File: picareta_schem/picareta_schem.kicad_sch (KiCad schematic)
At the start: 0 parts

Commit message: powertrain
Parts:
- added M1, M2, M3: Motor_DC, symbol Motor:Motor_DC
- added U1, U2, U3: ~, symbol ACC26:ESC
- added U4: ~, symbol library_pic_powertrain:PDB

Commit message: Updat Component's Format
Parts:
- added ADS1220: (no value), symbol Library_Laura_PIC:ADS1220
- added FLC3-1: (no value), symbol Library_Laura_PIC:FLC3-70
- added FLIR_LEPTON_CAMERA1, FLIR_LEPTON_CAMERA2: (no value), symbol Library_Laura_PIC:FLIR_Lepton_250-0577-00_DS_1-2021
- added JetsonOrinNX8GB1: (no value), symbol Library_Laura_PIC:Jetson_Orin_NX_8GB
- U1, U2, U3, U4: value ~ -> (none)

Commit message: Place Components On Schematic
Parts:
- added JetsonOrinNX8GB2: (no value), symbol Library_Laura_PIC:Jetson_Orin_NX_8GB
- added M10Q1: (no value), symbol Library_Laura_PIC:M10Q5883
- added MatekH743-WLITE1: (no value), symbol Library_Laura_PIC:Matek_H743-WLITE
- added RM-2450-12M1: (no value), symbol Library_Laura_PIC:RM-2450-12M3
- added SENTERA_6X_CAMERA1: (no value), symbol Library_Laura_PIC:SENTERA_6X_CAMERA

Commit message: Schematics progress with adjustments on component's pin placement
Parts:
- removed FLIR_LEPTON_CAMERA2: (no value), symbol Library_Laura_PIC:FLIR_Lepton_250-0577-00_DS_1-2021
- removed JetsonOrinNX8GB2: (no value), symbol Library_Laura_PIC:Jetson_Orin_NX_8GB
- added JetsonOrinNX8GB2: (no value), symbol Library_Laura_PIC:Jetson_Orin_NX_8GB_1
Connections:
- net 5V: now reaches U4. (BAT-)
- net 5V: now also ADS1220. (AIN3), FLIR_LEPTON_CAMERA1.2 (PWR_IN), M10Q1. (5V), MatekH743-WLITE1. (GND), RM-2450-12M1. (VDD)
- net SPI_CLK: now reaches ADS1220. (AIN3)
- net SPI_CLK: now also FLIR_LEPTON_CAMERA1.7 (SPI_CLK), MatekH743-WLITE1. (GND), JetsonOrinNX8GB2.91 (SPI0_SCK_)
- net SPI_MOSI: now reaches MatekH743-WLITE1. (GND)
- net SPI_MOSI: now also JetsonOrinNX8GB2.89 (SPI0_MOSI_)
- net GND: now reaches FLIR_LEPTON_CAMERA1.1 (GND)
- net GND: now also ADS1220. (AIN3), FLC3-1. (Z_A3), FLIR_LEPTON_CAMERA1.19 (GND), M10Q1. (5V), MatekH743-WLITE1. (GND), RM-2450-12M1. (VDD), SENTERA_6X_CAMERA1. (VDD-), JetsonOrinNX8GB2.247 (GND), JetsonOrinNX8GB2.249 (GND), JetsonOrinNX8GB2.251 (VDD_IN), JetsonOrinNX8GB2.253 (VDD_IN)
- net at FLIR_LEPTON_CAMERA1.10 (SPI_CS): now also ADS1220. (AIN3), JetsonOrinNX8GB2.97 (SPI0_CS1)
- new net: JetsonOrinNX8GB2.109 (USB0_D_N), RM-2450-12M1. (VDD)
- new net: JetsonOrinNX8GB2.111 (USB0_D_P), RM-2450-12M1. (VDD)
- new net: JetsonOrinNX8GB2.95 (SPI0_CS0), MatekH743-WLITE1. (GND)
- new net: M10Q1. (5V), MatekH743-WLITE1. (GND) (x4)
- new net: ADS1220. (AIN3), FLC3-1. (Z_A3) (x3)
- new net: JetsonOrinNX8GB2.184 (GBE_MDI0_N), SENTERA_6X_CAMERA1. (VDD-)
- new net: JetsonOrinNX8GB2.186 (GBE_MDI0_P), SENTERA_6X_CAMERA1. (VDD-)
- new net: JetsonOrinNX8GB2.188 (GBE_LED_LINK), SENTERA_6X_CAMERA1. (VDD-)
- new net: JetsonOrinNX8GB2.190 (GBE_MDI1_N), SENTERA_6X_CAMERA1. (VDD-)
- new net: JetsonOrinNX8GB2.192 (GBE_MDI1_P), SENTERA_6X_CAMERA1. (VDD-)
- new net: JetsonOrinNX8GB2.194 (GBE_LED_ACT), SENTERA_6X_CAMERA1. (VDD-)
- new net: JetsonOrinNX8GB2.196 (GBE_MDI2_N), SENTERA_6X_CAMERA1. (VDD-)
- new net: JetsonOrinNX8GB2.198 (GBE_MDI2_P), SENTERA_6X_CAMERA1. (VDD-)
- new net: JetsonOrinNX8GB2.202 (GBE_MDI3_N), SENTERA_6X_CAMERA1. (VDD-)
- new net: JetsonOrinNX8GB2.204 (GBE_MDI3_P), SENTERA_6X_CAMERA1. (VDD-)
- new net 12V: FLC3-1. (Z_A3), JetsonOrinNX8GB2.237 (POWER_EN), MatekH743-WLITE1. (GND), SENTERA_6X_CAMERA1. (VDD-)
- new net 3V3: MatekH743-WLITE1. (GND)
- new net SPI_MISO: JetsonOrinNX8GB2.93 (SPI0_MISO_), MatekH743-WLITE1. (GND)
- no-connect marks 0 -> 9
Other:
- note added: "Faltam os 12V e 3V3"
- title: (none) -> Drone Avionic's Schematic
- moved on the sheet: M1, M10Q1, M2, M3, SENTERA_6X_CAMERA1

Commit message: Lowkirkenuily Good Avionics Schematic
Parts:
- removed FLIR_LEPTON_CAMERA1: (no value), symbol Library_Laura_PIC:FLIR_Lepton_250-0577-00_DS_1-2021
- removed M10Q1: (no value), symbol Library_Laura_PIC:M10Q5883
- removed SENTERA_6X_CAMERA1: (no value), symbol Library_Laura_PIC:SENTERA_6X_CAMERA
- added FLIR_LEPTON_CAMERA: (no value), symbol Library_Laura_PIC:FLIR_Lepton_250-0577-00_DS_1-2021
- added M10Q5883: (no value), symbol Library_Laura_PIC:M10Q5883
- added SENTERA_6X_CAMERA: (no value), symbol Library_Laura_PIC:SENTERA_6X_CAMERA
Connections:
- net 12V: now also FLIR_LEPTON_CAMERA.16 (VCC12), SENTERA_6X_CAMERA. (VDD-)
- net 5V: now also FLIR_LEPTON_CAMERA.2 (PWR_IN), M10Q5883. (GND)
- net GND: now also FLIR_LEPTON_CAMERA.1 (GND), FLIR_LEPTON_CAMERA.19 (GND), M10Q5883. (GND), SENTERA_6X_CAMERA. (VDD-)
- net SPI_CLK: now also FLIR_LEPTON_CAMERA.7 (SPI_CLK)
- net SPI_MISO: now also ADS1220. (AIN3), FLIR_LEPTON_CAMERA.12 (SPI_MISO)
- net SPI_MOSI: now also ADS1220. (AIN3), FLIR_LEPTON_CAMERA.9 (SPI_MOSI)
- net PAYLOAD_SELECT: now reaches ADS1220. (AIN3), JetsonOrinNX8GB2.97 (SPI0_CS1)
- net PAYLOAD_SELECT: now also FLIR_LEPTON_CAMERA.10 (SPI_CS)
- net CAM_PWDN: now reaches JetsonOrinNX8GB2.114 (CAM0_PWDN_)
- net CAM_PWDN: now also FLIR_LEPTON_CAMERA.20 (PW_DWN_L)
- net CAM_MCLK: now reaches JetsonOrinNX8GB2.116 (CAM0_MCLK_)
- net CAM_MCLK: now also FLIR_LEPTON_CAMERA.18 (MASTER_CLK)
- net at JetsonOrinNX8GB2.184 (GBE_MDI0_N): now also SENTERA_6X_CAMERA. (VDD-)
- net at JetsonOrinNX8GB2.186 (GBE_MDI0_P): now also SENTERA_6X_CAMERA. (VDD-)
- net at JetsonOrinNX8GB2.188 (GBE_LED_LINK): now also SENTERA_6X_CAMERA. (VDD-)
- net at JetsonOrinNX8GB2.190 (GBE_MDI1_N): now also SENTERA_6X_CAMERA. (VDD-)
- net at JetsonOrinNX8GB2.192 (GBE_MDI1_P): now also SENTERA_6X_CAMERA. (VDD-)
- net at JetsonOrinNX8GB2.194 (GBE_LED_ACT): now also SENTERA_6X_CAMERA. (VDD-)
- net at JetsonOrinNX8GB2.196 (GBE_MDI2_N): now also SENTERA_6X_CAMERA. (VDD-)
- net at JetsonOrinNX8GB2.198 (GBE_MDI2_P): now also SENTERA_6X_CAMERA. (VDD-)
- net at JetsonOrinNX8GB2.202 (GBE_MDI3_N): now also SENTERA_6X_CAMERA. (VDD-)
- net at JetsonOrinNX8GB2.204 (GBE_MDI3_P): now also SENTERA_6X_CAMERA. (VDD-)
- new net: ADS1220. (AIN3), FLC3-1. (Z_A3) (x3)
- new net: M10Q5883. (GND), MatekH743-WLITE1. (GND) (x4)
- no-connect marks 9 -> 21
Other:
- note added: "PAYLOAD"
- moved on the sheet: FLC3-1, M1, M2, M3, MatekH743-WLITE1

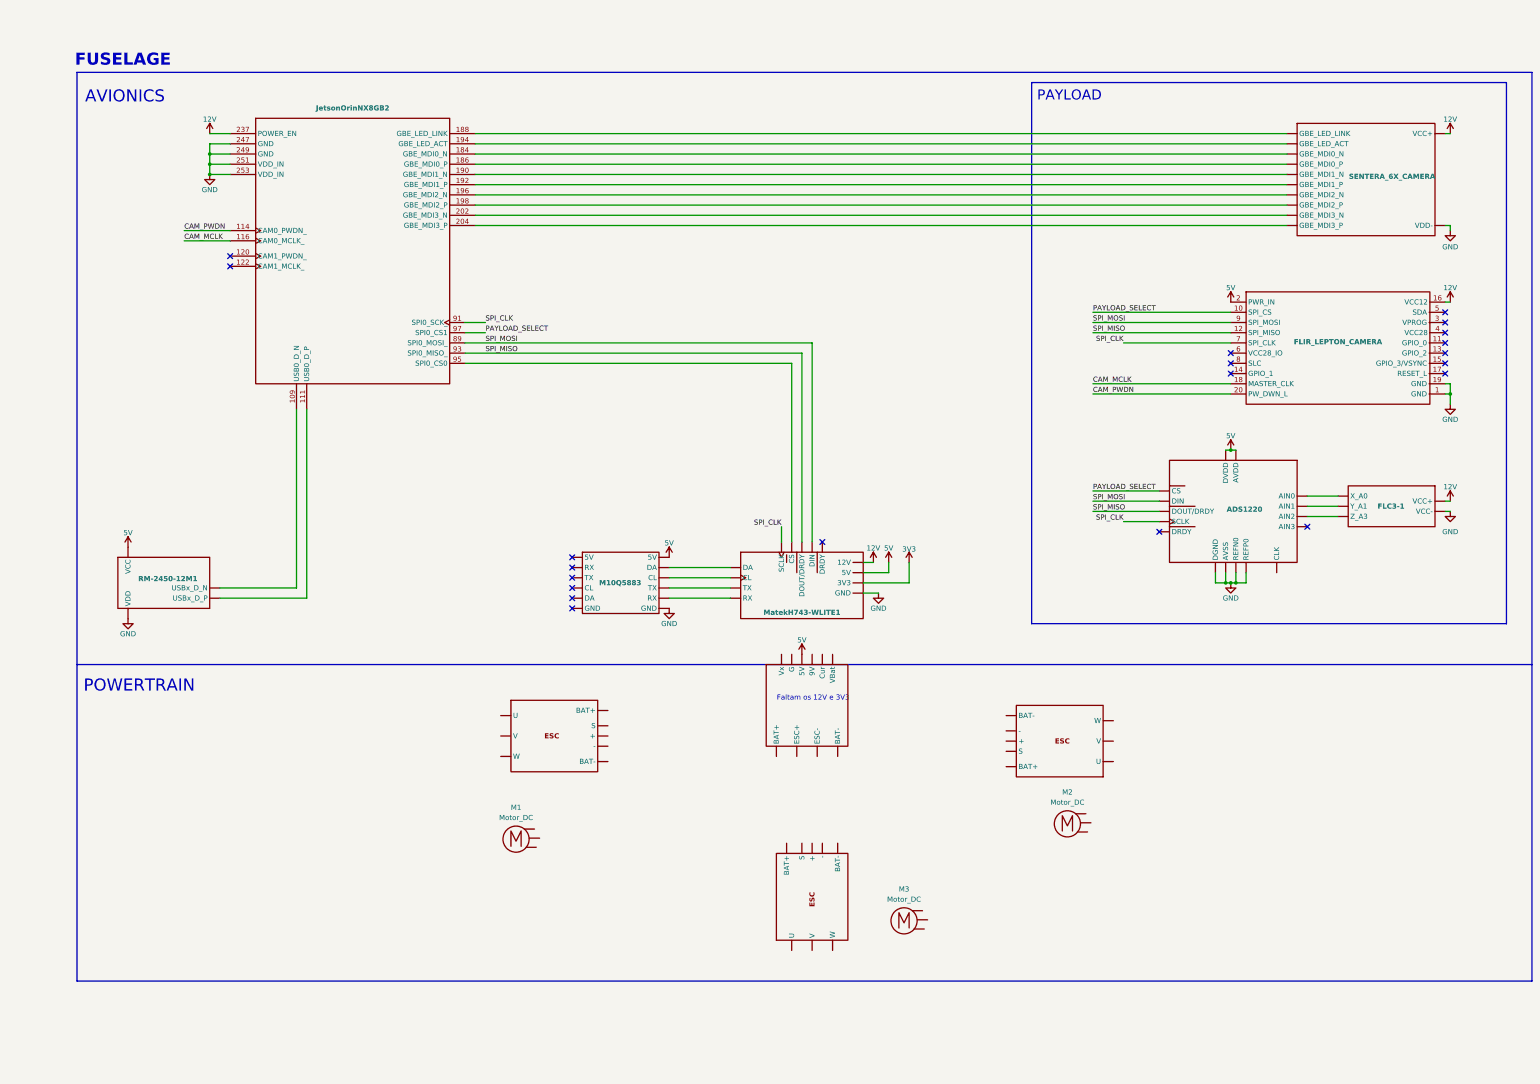
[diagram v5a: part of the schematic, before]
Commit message: Joined Powertrain's Schematic
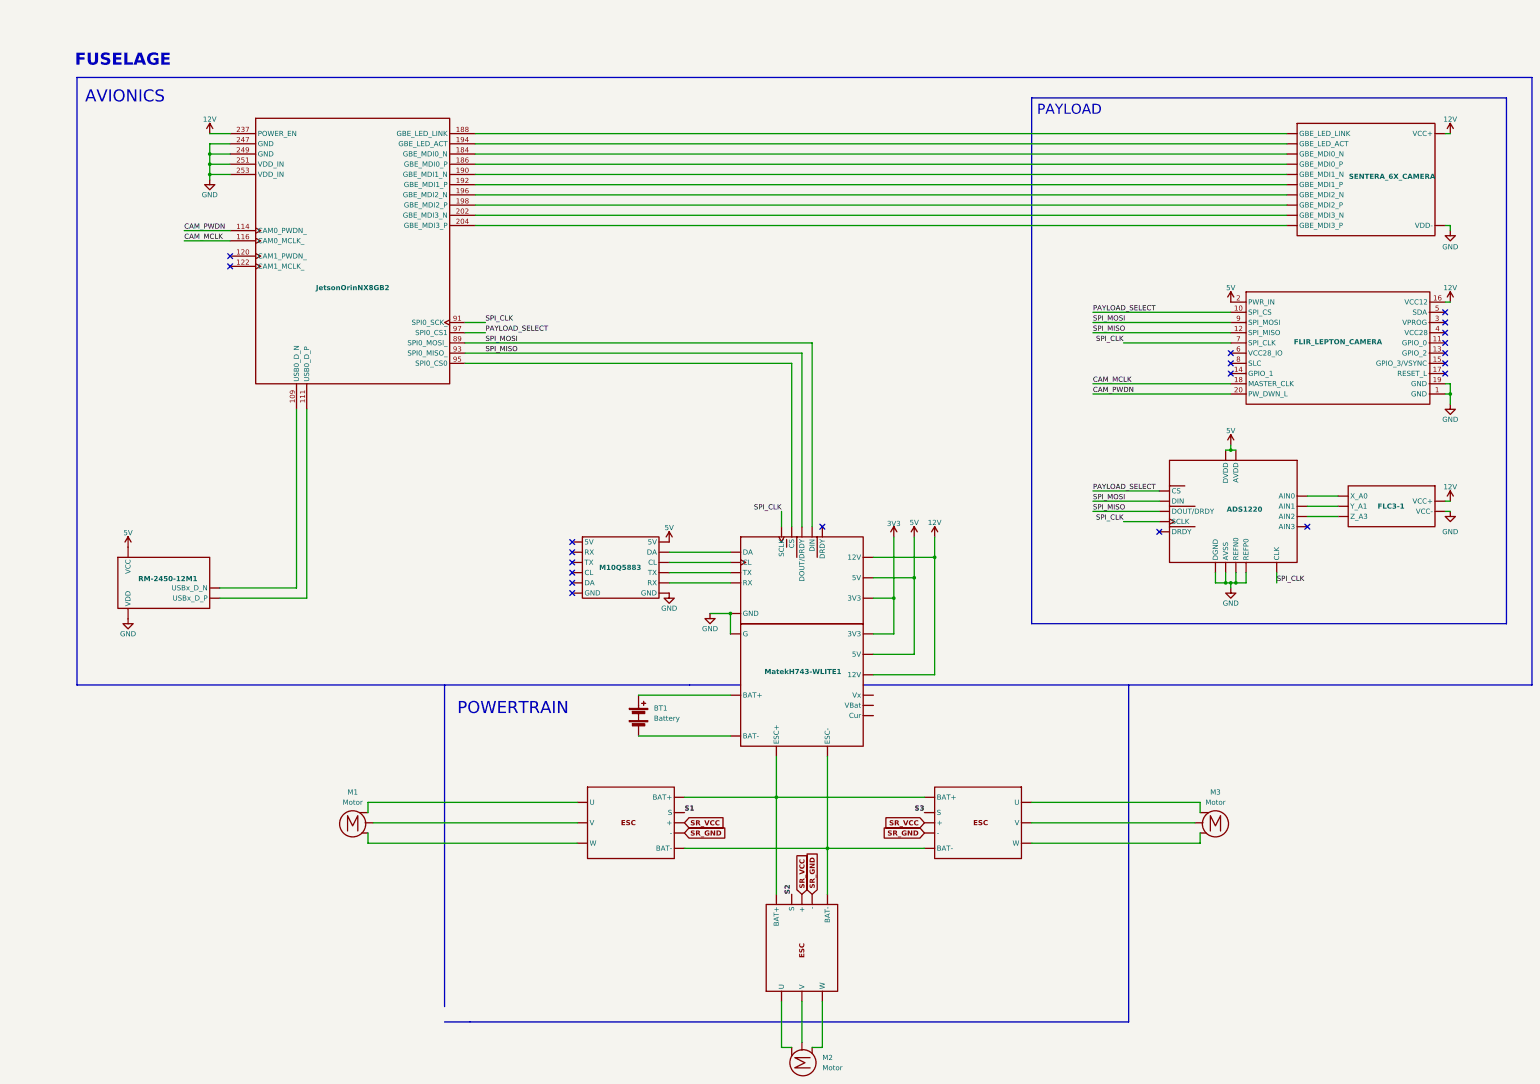
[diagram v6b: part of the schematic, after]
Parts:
- removed M1, M2, M3: Motor_DC, symbol Motor:Motor_DC
- removed U2: (no value), symbol ACC26:ESC
- added BT1: Battery, symbol Device:Battery
- added M1, M2, M3: Motor, symbol Library_Laura_PIC:Motor
- added U5: (no value), symbol Library_Laura_PIC:ESC
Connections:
- net 12V: now also U4. (Cur)
- net 3V3: now also U4. (Cur)
- net GND: now also U4. (Cur)
- net SR_VCC: now reaches U1. (BAT-)
- net SR_VCC: now also U3. (BAT-), U5. (W)
- new net: M3., U5. (W) (x3)
- new net: M1., U1. (BAT-) (x3)
- new net: ADS1220. (AIN3), FLC3-1. (Z_A3) (x3)
- new net: U1. (BAT-), U3. (BAT-), U4. (Cur), U5. (W) (x2)
- new net: BT1.1 (+), U4. (Cur)
- new net: BT1.2 (-), U4. (Cur)
- new net: M2., U3. (BAT-) (x3)
- new net: M10Q5883. (GND), MatekH743-WLITE1. (3V3) (x4)
- new net S1: U1. (BAT-)
- new net S2: U3. (BAT-)
- new net S3: U5. (W)
- new net SR_GND: U1. (BAT-), U3. (BAT-), U5. (W)
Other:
- note removed: "Faltam os 12V e 3V3"
- moved on the sheet: M10Q5883

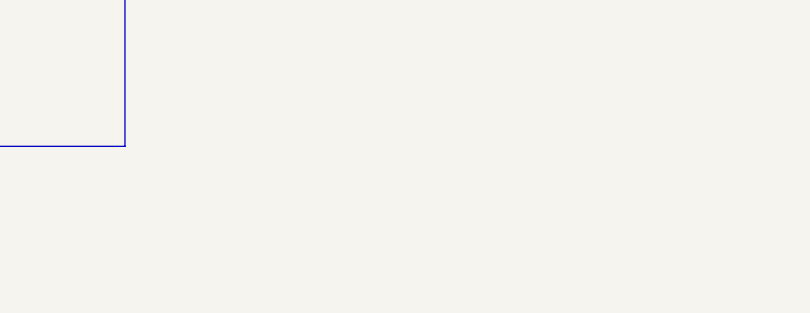
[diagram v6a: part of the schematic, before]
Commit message: Added Current PDF Schematic
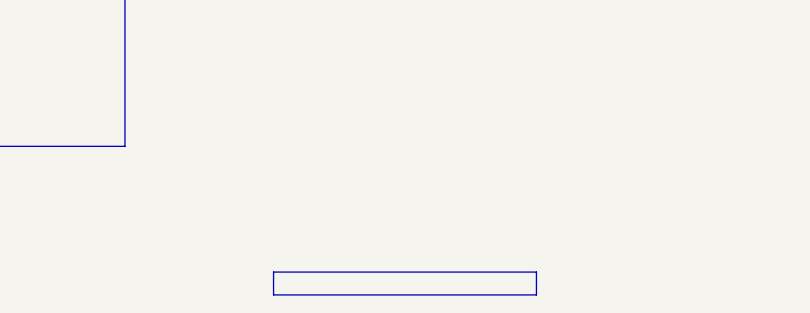
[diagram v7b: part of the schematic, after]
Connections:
- new net: M3., U5. (W) (x2)
- new net: M1., U1. (BAT-) (x2)
- new net: ADS1220. (AIN3), FLC3-1. (Z_A3) (x3)
- new net: U1. (BAT-), U3. (BAT-), U4. (Cur), U5. (W) (x2)
- new net: M2., U3. (BAT-) (x2)
- new net: M10Q5883. (GND), MatekH743-WLITE1. (3V3) (x4)
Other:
- company: (none) -> Omniscan
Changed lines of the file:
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@@
 	(title_block
 		(title "Drone Avionic's Schematic")
+		(date "May 2026")
+		(company "Omniscan")
 	)
 	(rectangle
@@
 		)
 	)
+	(rectangle
+		(start 307.34 271.78)
+		(end 336.55 274.32)
+		(stroke
+			(width 0)
+			(type solid)
+			(color 255 247 255 1)
+		)
+		(fill
+			(type color)
+			(color 255 250 255 1)
+		)
+	)

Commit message: Aesthetics
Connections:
- new net: M3., U5. (W) (x2)
- new net: M1., U1. (BAT-) (x2)
- new net: ADS1220. (AIN3), FLC3-1. (Z_A3) (x3)
- new net: U1. (BAT-), U3. (BAT-), U4. (Cur), U5. (W) (x2)
- new net: M2., U3. (BAT-) (x2)
- new net: M10Q5883. (GND), MatekH743-WLITE1. (3V3) (x4)
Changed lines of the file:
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@@
+		)
+	)
+	(polyline
+		(pts
+			(xy 120.65 254) (xy 120.65 257.81)
+		)
+		(stroke
+			(width 0)
+			(type default)
 		)
 	)
